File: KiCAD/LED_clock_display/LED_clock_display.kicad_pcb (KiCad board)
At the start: 2 copper layers, 228.6 x 228.6 mm, 392 parts, among them J1 CONN_2X10, U1 ICM7218A, U2 ICM7218A, U3 ICM7218A, U4 ICM7218A, U5 ICM7218A, U6 ICM7218A, U7 74HC138, U8 74LS244, U9 74LS125

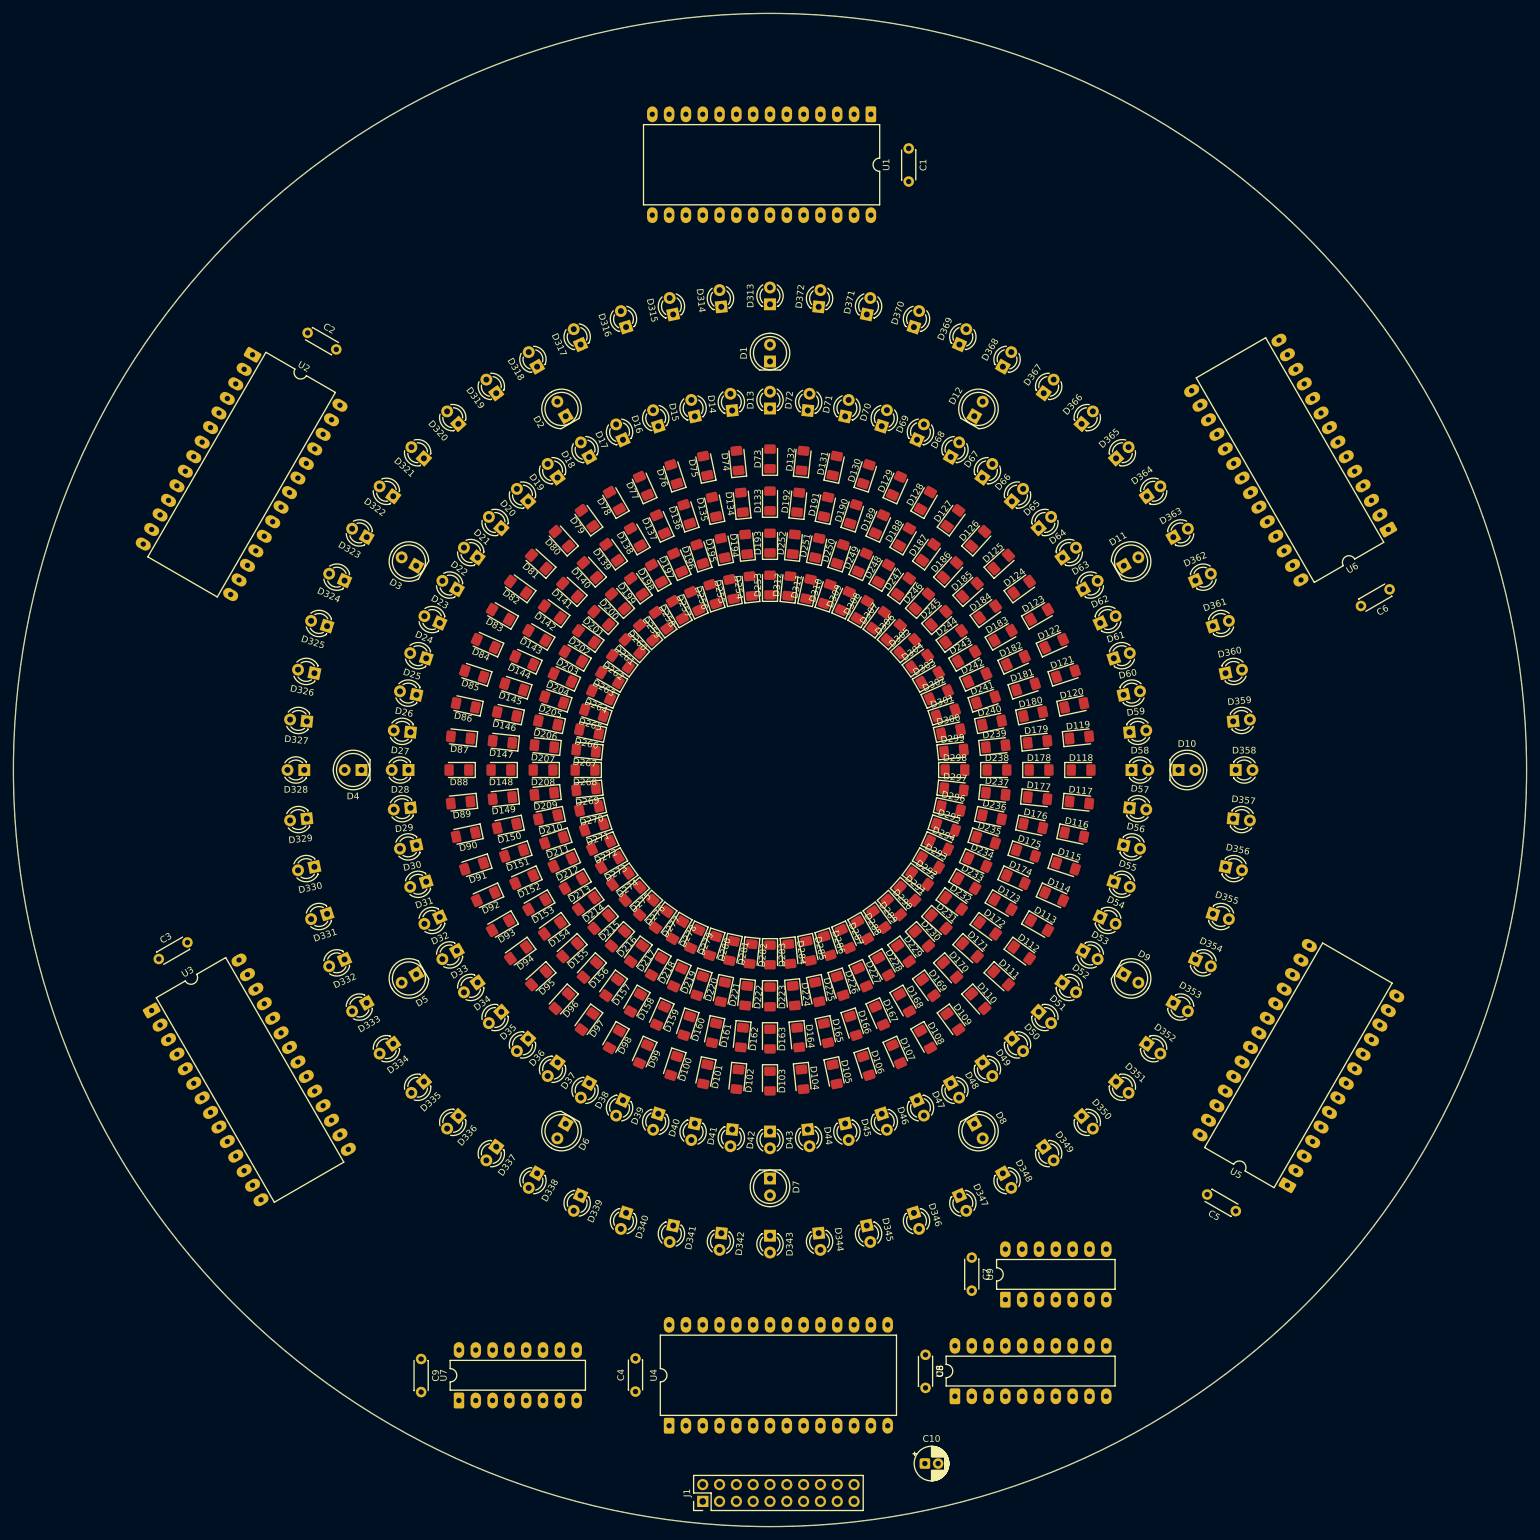
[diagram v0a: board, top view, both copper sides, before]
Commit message: Split into two boards
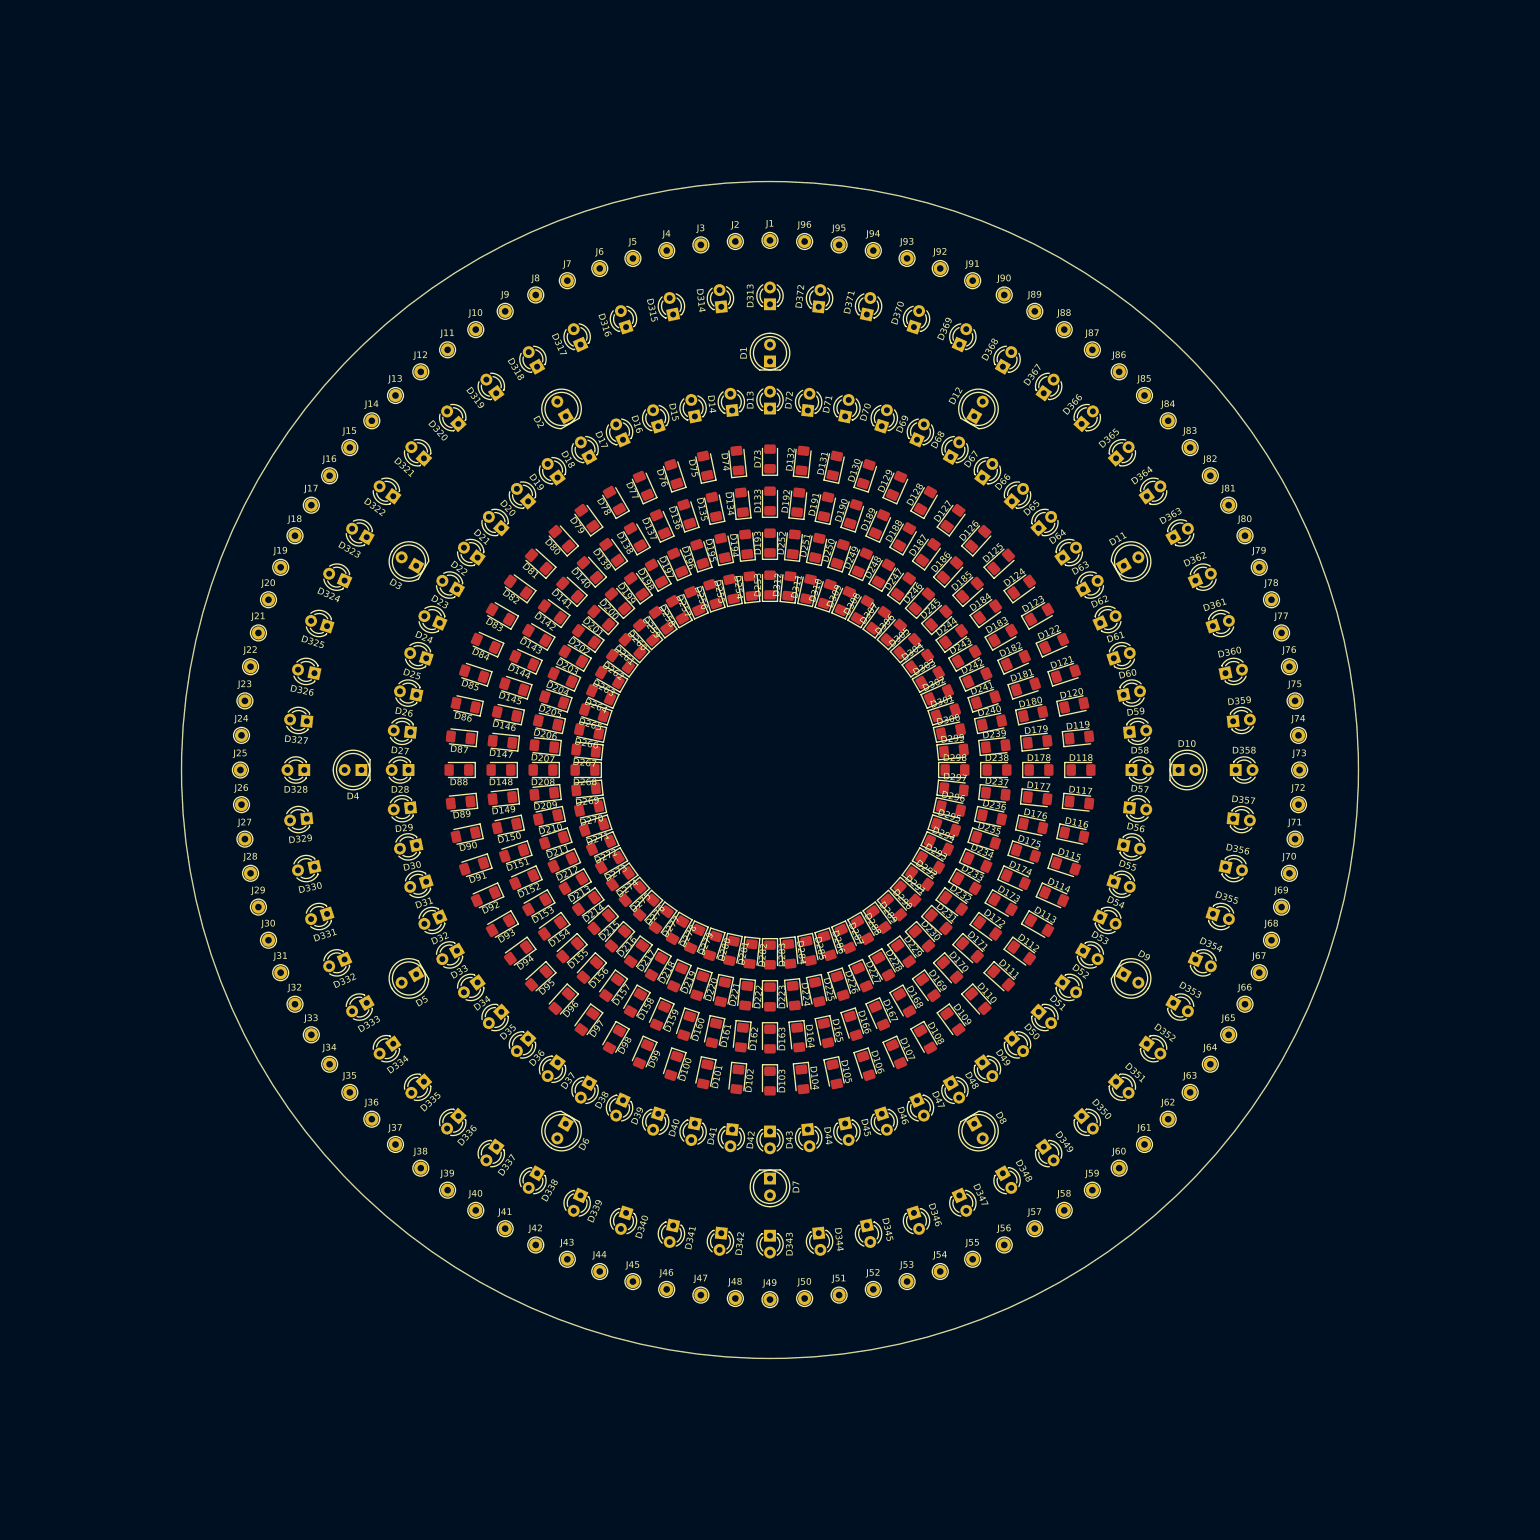
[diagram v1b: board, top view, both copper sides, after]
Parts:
- removed C1, C2, C3, C4, C5, C6, C7, C8, C9: 0.1uF, Capacitor_THT:C_Disc_D4.3mm_W1.9mm_P5.00mm
- removed C10: 33uF, Capacitor_THT:CP_Radial_D5.0mm_P2.00mm
- removed U1, U2, U3, U4, U5, U6: ICM7218A, Package_DIP:DIP-28_W15.24mm_LongPads
- removed U7: 74HC138, Package_DIP:DIP-16_W7.62mm_LongPads
- removed U8: 74LS244, Package_DIP:DIP-20_W7.62mm_LongPads
- removed U9: 74LS125, Package_DIP:DIP-14_W7.62mm_LongPads
- added J10: PIN, TestPoint:TestPoint_THTPad_D2.0mm_Drill1.0mm, F.Cu at (209.5, 111.3)
- added J11: PIN, TestPoint:TestPoint_THTPad_D2.0mm_Drill1.0mm, F.Cu at (205.3, 114.3)
- added J12: PIN, TestPoint:TestPoint_THTPad_D2.0mm_Drill1.0mm, F.Cu at (201.2, 117.6)
- added J13: PIN, TestPoint:TestPoint_THTPad_D2.0mm_Drill1.0mm, F.Cu at (197.4, 121.2)
- added J14: PIN, TestPoint:TestPoint_THTPad_D2.0mm_Drill1.0mm, F.Cu at (193.8, 125.0)
- added J15: PIN, TestPoint:TestPoint_THTPad_D2.0mm_Drill1.0mm, F.Cu at (190.5, 129.1)
- added J16: PIN, TestPoint:TestPoint_THTPad_D2.0mm_Drill1.0mm, F.Cu at (187.5, 133.3)
- added J17: PIN, TestPoint:TestPoint_THTPad_D2.0mm_Drill1.0mm, F.Cu at (184.7, 137.8)
- added J18: PIN, TestPoint:TestPoint_THTPad_D2.0mm_Drill1.0mm, F.Cu at (182.2, 142.4)
- added J19: PIN, TestPoint:TestPoint_THTPad_D2.0mm_Drill1.0mm, F.Cu at (180.1, 147.2)
- added J2: PIN, TestPoint:TestPoint_THTPad_D2.0mm_Drill1.0mm, F.Cu at (248.8, 98.0)
- added J20: PIN, TestPoint:TestPoint_THTPad_D2.0mm_Drill1.0mm, F.Cu at (178.2, 152.1)
- added J21: PIN, TestPoint:TestPoint_THTPad_D2.0mm_Drill1.0mm, F.Cu at (176.7, 157.1)
- added J22: PIN, TestPoint:TestPoint_THTPad_D2.0mm_Drill1.0mm, F.Cu at (175.5, 162.2)
- added J23: PIN, TestPoint:TestPoint_THTPad_D2.0mm_Drill1.0mm, F.Cu at (174.7, 167.4)
- added J24: PIN, TestPoint:TestPoint_THTPad_D2.0mm_Drill1.0mm, F.Cu at (174.2, 172.6)
- added J25: PIN, TestPoint:TestPoint_THTPad_D2.0mm_Drill1.0mm, F.Cu at (174.0, 177.8)
- added J26: PIN, TestPoint:TestPoint_THTPad_D2.0mm_Drill1.0mm, F.Cu at (174.2, 183.0)
- added J27: PIN, TestPoint:TestPoint_THTPad_D2.0mm_Drill1.0mm, F.Cu at (174.7, 188.2)
- added J28: PIN, TestPoint:TestPoint_THTPad_D2.0mm_Drill1.0mm, F.Cu at (175.5, 193.4)
- added J29: PIN, TestPoint:TestPoint_THTPad_D2.0mm_Drill1.0mm, F.Cu at (176.7, 198.5)
- added J3: PIN, TestPoint:TestPoint_THTPad_D2.0mm_Drill1.0mm, F.Cu at (243.6, 98.5)
- added J30: PIN, TestPoint:TestPoint_THTPad_D2.0mm_Drill1.0mm, F.Cu at (178.2, 203.5)
- added J31: PIN, TestPoint:TestPoint_THTPad_D2.0mm_Drill1.0mm, F.Cu at (180.1, 208.4)
- added J32: PIN, TestPoint:TestPoint_THTPad_D2.0mm_Drill1.0mm, F.Cu at (182.2, 213.2)
- added J33: PIN, TestPoint:TestPoint_THTPad_D2.0mm_Drill1.0mm, F.Cu at (184.7, 217.8)
- added J34: PIN, TestPoint:TestPoint_THTPad_D2.0mm_Drill1.0mm, F.Cu at (187.5, 222.3)
- added J35: PIN, TestPoint:TestPoint_THTPad_D2.0mm_Drill1.0mm, F.Cu at (190.5, 226.5)
- added J36: PIN, TestPoint:TestPoint_THTPad_D2.0mm_Drill1.0mm, F.Cu at (193.8, 230.6)
- added J37: PIN, TestPoint:TestPoint_THTPad_D2.0mm_Drill1.0mm, F.Cu at (197.4, 234.4)
- added J38: PIN, TestPoint:TestPoint_THTPad_D2.0mm_Drill1.0mm, F.Cu at (201.2, 238.0)
- added J39: PIN, TestPoint:TestPoint_THTPad_D2.0mm_Drill1.0mm, F.Cu at (205.3, 241.3)
- added J4: PIN, TestPoint:TestPoint_THTPad_D2.0mm_Drill1.0mm, F.Cu at (238.4, 99.3)
- added J40: PIN, TestPoint:TestPoint_THTPad_D2.0mm_Drill1.0mm, F.Cu at (209.5, 244.3)
- added J41: PIN, TestPoint:TestPoint_THTPad_D2.0mm_Drill1.0mm, F.Cu at (214.0, 247.1)
- added J42: PIN, TestPoint:TestPoint_THTPad_D2.0mm_Drill1.0mm, F.Cu at (218.6, 249.6)
- added J43: PIN, TestPoint:TestPoint_THTPad_D2.0mm_Drill1.0mm, F.Cu at (223.4, 251.7)
- added J44: PIN, TestPoint:TestPoint_THTPad_D2.0mm_Drill1.0mm, F.Cu at (228.3, 253.6)
- added J45: PIN, TestPoint:TestPoint_THTPad_D2.0mm_Drill1.0mm, F.Cu at (233.3, 255.1)
- added J46: PIN, TestPoint:TestPoint_THTPad_D2.0mm_Drill1.0mm, F.Cu at (238.4, 256.3)
- added J47: PIN, TestPoint:TestPoint_THTPad_D2.0mm_Drill1.0mm, F.Cu at (243.6, 257.1)
- added J48: PIN, TestPoint:TestPoint_THTPad_D2.0mm_Drill1.0mm, F.Cu at (248.8, 257.6)
- added J49: PIN, TestPoint:TestPoint_THTPad_D2.0mm_Drill1.0mm, F.Cu at (254.0, 257.8)
- added J5: PIN, TestPoint:TestPoint_THTPad_D2.0mm_Drill1.0mm, F.Cu at (233.3, 100.5)
- added J50: PIN, TestPoint:TestPoint_THTPad_D2.0mm_Drill1.0mm, F.Cu at (259.2, 257.6)
- added J51: PIN, TestPoint:TestPoint_THTPad_D2.0mm_Drill1.0mm, F.Cu at (264.4, 257.1)
- added J52: PIN, TestPoint:TestPoint_THTPad_D2.0mm_Drill1.0mm, F.Cu at (269.6, 256.3)
- added J53: PIN, TestPoint:TestPoint_THTPad_D2.0mm_Drill1.0mm, F.Cu at (274.7, 255.1)
- added J54: PIN, TestPoint:TestPoint_THTPad_D2.0mm_Drill1.0mm, F.Cu at (279.7, 253.6)
- added J55: PIN, TestPoint:TestPoint_THTPad_D2.0mm_Drill1.0mm, F.Cu at (284.6, 251.7)
- added J56: PIN, TestPoint:TestPoint_THTPad_D2.0mm_Drill1.0mm, F.Cu at (289.4, 249.6)
- added J57: PIN, TestPoint:TestPoint_THTPad_D2.0mm_Drill1.0mm, F.Cu at (294.0, 247.1)
- added J58: PIN, TestPoint:TestPoint_THTPad_D2.0mm_Drill1.0mm, F.Cu at (298.5, 244.3)
- added J59: PIN, TestPoint:TestPoint_THTPad_D2.0mm_Drill1.0mm, F.Cu at (302.7, 241.3)
- added J6: PIN, TestPoint:TestPoint_THTPad_D2.0mm_Drill1.0mm, F.Cu at (228.3, 102.0)
- added J60: PIN, TestPoint:TestPoint_THTPad_D2.0mm_Drill1.0mm, F.Cu at (306.8, 238.0)
- added J61: PIN, TestPoint:TestPoint_THTPad_D2.0mm_Drill1.0mm, F.Cu at (310.6, 234.4)
- added J62: PIN, TestPoint:TestPoint_THTPad_D2.0mm_Drill1.0mm, F.Cu at (314.2, 230.6)
- added J63: PIN, TestPoint:TestPoint_THTPad_D2.0mm_Drill1.0mm, F.Cu at (317.5, 226.5)
- added J64: PIN, TestPoint:TestPoint_THTPad_D2.0mm_Drill1.0mm, F.Cu at (320.5, 222.3)
- added J65: PIN, TestPoint:TestPoint_THTPad_D2.0mm_Drill1.0mm, F.Cu at (323.3, 217.8)
- added J66: PIN, TestPoint:TestPoint_THTPad_D2.0mm_Drill1.0mm, F.Cu at (325.8, 213.2)
- added J67: PIN, TestPoint:TestPoint_THTPad_D2.0mm_Drill1.0mm, F.Cu at (327.9, 208.4)
- added J68: PIN, TestPoint:TestPoint_THTPad_D2.0mm_Drill1.0mm, F.Cu at (329.8, 203.5)
- added J69: PIN, TestPoint:TestPoint_THTPad_D2.0mm_Drill1.0mm, F.Cu at (331.3, 198.5)
- added J7: PIN, TestPoint:TestPoint_THTPad_D2.0mm_Drill1.0mm, F.Cu at (223.4, 103.9)
- added J70: PIN, TestPoint:TestPoint_THTPad_D2.0mm_Drill1.0mm, F.Cu at (332.5, 193.4)
- added J71: PIN, TestPoint:TestPoint_THTPad_D2.0mm_Drill1.0mm, F.Cu at (333.3, 188.2)
- added J72: PIN, TestPoint:TestPoint_THTPad_D2.0mm_Drill1.0mm, F.Cu at (333.8, 183.0)
- added J73: PIN, TestPoint:TestPoint_THTPad_D2.0mm_Drill1.0mm, F.Cu at (334.0, 177.8)
- added J74: PIN, TestPoint:TestPoint_THTPad_D2.0mm_Drill1.0mm, F.Cu at (333.8, 172.6)
- added J75: PIN, TestPoint:TestPoint_THTPad_D2.0mm_Drill1.0mm, F.Cu at (333.3, 167.4)
- added J76: PIN, TestPoint:TestPoint_THTPad_D2.0mm_Drill1.0mm, F.Cu at (332.5, 162.2)
- added J77: PIN, TestPoint:TestPoint_THTPad_D2.0mm_Drill1.0mm, F.Cu at (331.3, 157.1)
- added J78: PIN, TestPoint:TestPoint_THTPad_D2.0mm_Drill1.0mm, F.Cu at (329.8, 152.1)
- added J79: PIN, TestPoint:TestPoint_THTPad_D2.0mm_Drill1.0mm, F.Cu at (327.9, 147.2)
- added J8: PIN, TestPoint:TestPoint_THTPad_D2.0mm_Drill1.0mm, F.Cu at (218.6, 106.0)
- added J80: PIN, TestPoint:TestPoint_THTPad_D2.0mm_Drill1.0mm, F.Cu at (325.8, 142.4)
- added J81: PIN, TestPoint:TestPoint_THTPad_D2.0mm_Drill1.0mm, F.Cu at (323.3, 137.8)
- added J82: PIN, TestPoint:TestPoint_THTPad_D2.0mm_Drill1.0mm, F.Cu at (320.5, 133.3)
- added J83: PIN, TestPoint:TestPoint_THTPad_D2.0mm_Drill1.0mm, F.Cu at (317.5, 129.1)
- added J84: PIN, TestPoint:TestPoint_THTPad_D2.0mm_Drill1.0mm, F.Cu at (314.2, 125.0)
- added J85: PIN, TestPoint:TestPoint_THTPad_D2.0mm_Drill1.0mm, F.Cu at (310.6, 121.2)
- added J86: PIN, TestPoint:TestPoint_THTPad_D2.0mm_Drill1.0mm, F.Cu at (306.8, 117.6)
- added J87: PIN, TestPoint:TestPoint_THTPad_D2.0mm_Drill1.0mm, F.Cu at (302.7, 114.3)
- added J88: PIN, TestPoint:TestPoint_THTPad_D2.0mm_Drill1.0mm, F.Cu at (298.5, 111.3)
- added J89: PIN, TestPoint:TestPoint_THTPad_D2.0mm_Drill1.0mm, F.Cu at (294.0, 108.5)
- added J9: PIN, TestPoint:TestPoint_THTPad_D2.0mm_Drill1.0mm, F.Cu at (214.0, 108.5)
- added J90: PIN, TestPoint:TestPoint_THTPad_D2.0mm_Drill1.0mm, F.Cu at (289.4, 106.0)
- added J91: PIN, TestPoint:TestPoint_THTPad_D2.0mm_Drill1.0mm, F.Cu at (284.6, 103.9)
- added J92: PIN, TestPoint:TestPoint_THTPad_D2.0mm_Drill1.0mm, F.Cu at (279.7, 102.0)
- added J93: PIN, TestPoint:TestPoint_THTPad_D2.0mm_Drill1.0mm, F.Cu at (274.7, 100.5)
- added J94: PIN, TestPoint:TestPoint_THTPad_D2.0mm_Drill1.0mm, F.Cu at (269.6, 99.3)
- added J95: PIN, TestPoint:TestPoint_THTPad_D2.0mm_Drill1.0mm, F.Cu at (264.4, 98.5)
- added J96: PIN, TestPoint:TestPoint_THTPad_D2.0mm_Drill1.0mm, F.Cu at (259.2, 98.0)
- J1: value CONN_2X10 -> PIN; footprint Connector_PinHeader_2.54mm:PinHeader_2x10_P2.54mm_Vertical -> TestPoint:TestPoint_THTPad_D2.0mm_Drill1.0mm
- moved J1 190.8 mm to (254.0, 97.8), turned to 0 degrees
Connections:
- J1 pad 1: VCC -> /R7_X0
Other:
- board size 228.6 x 228.6 mm -> 177.8 x 177.8 mm
